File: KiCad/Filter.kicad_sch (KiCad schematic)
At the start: 25 parts, among them U5 TL074, U6 TL074

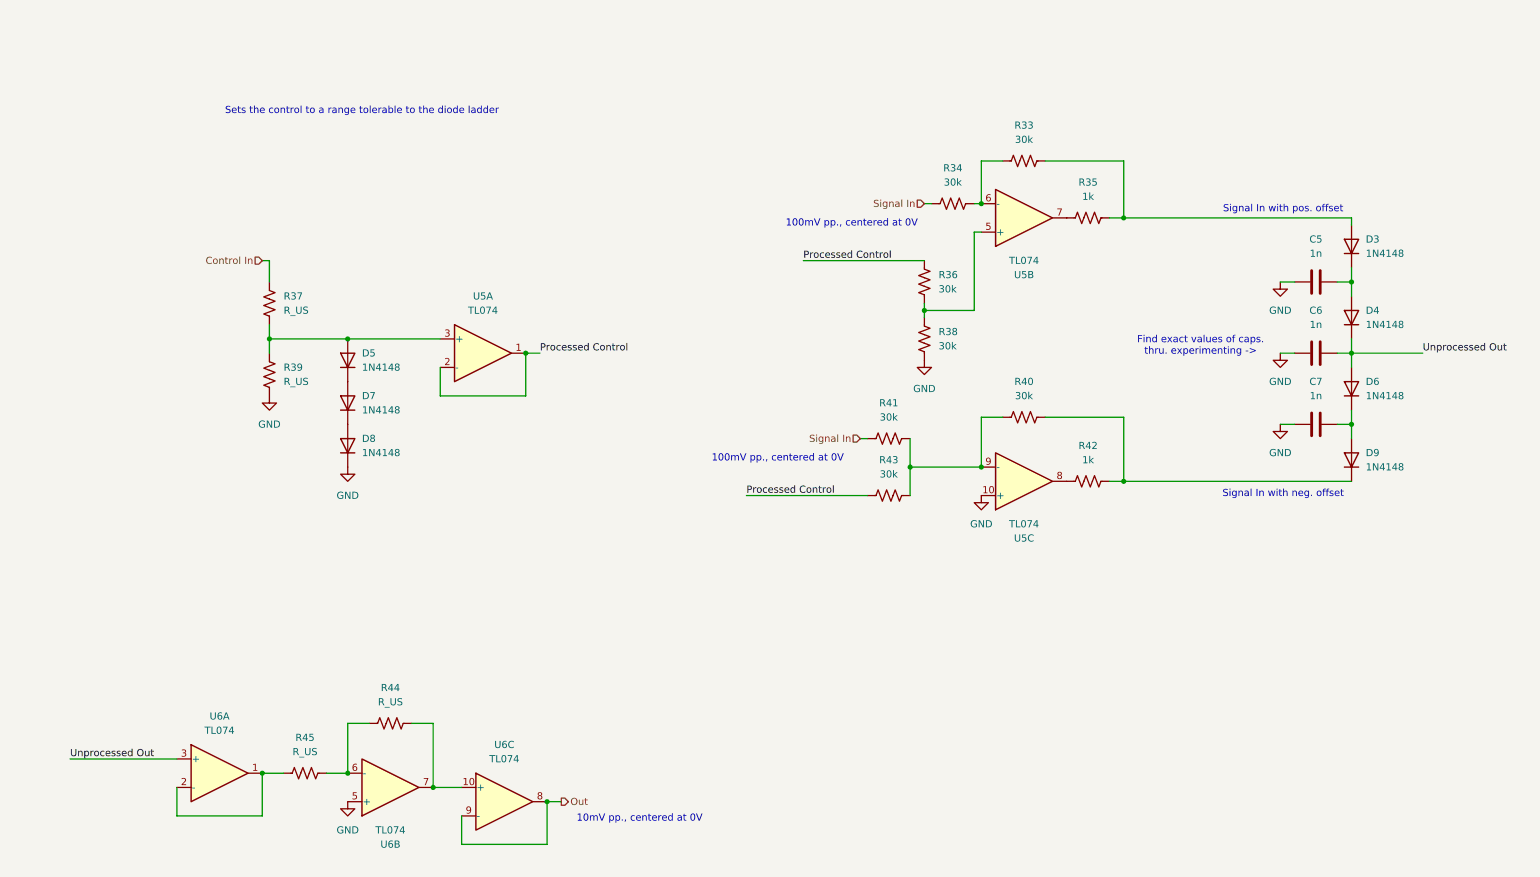
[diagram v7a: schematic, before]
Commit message: added potentiometer voltage control cct
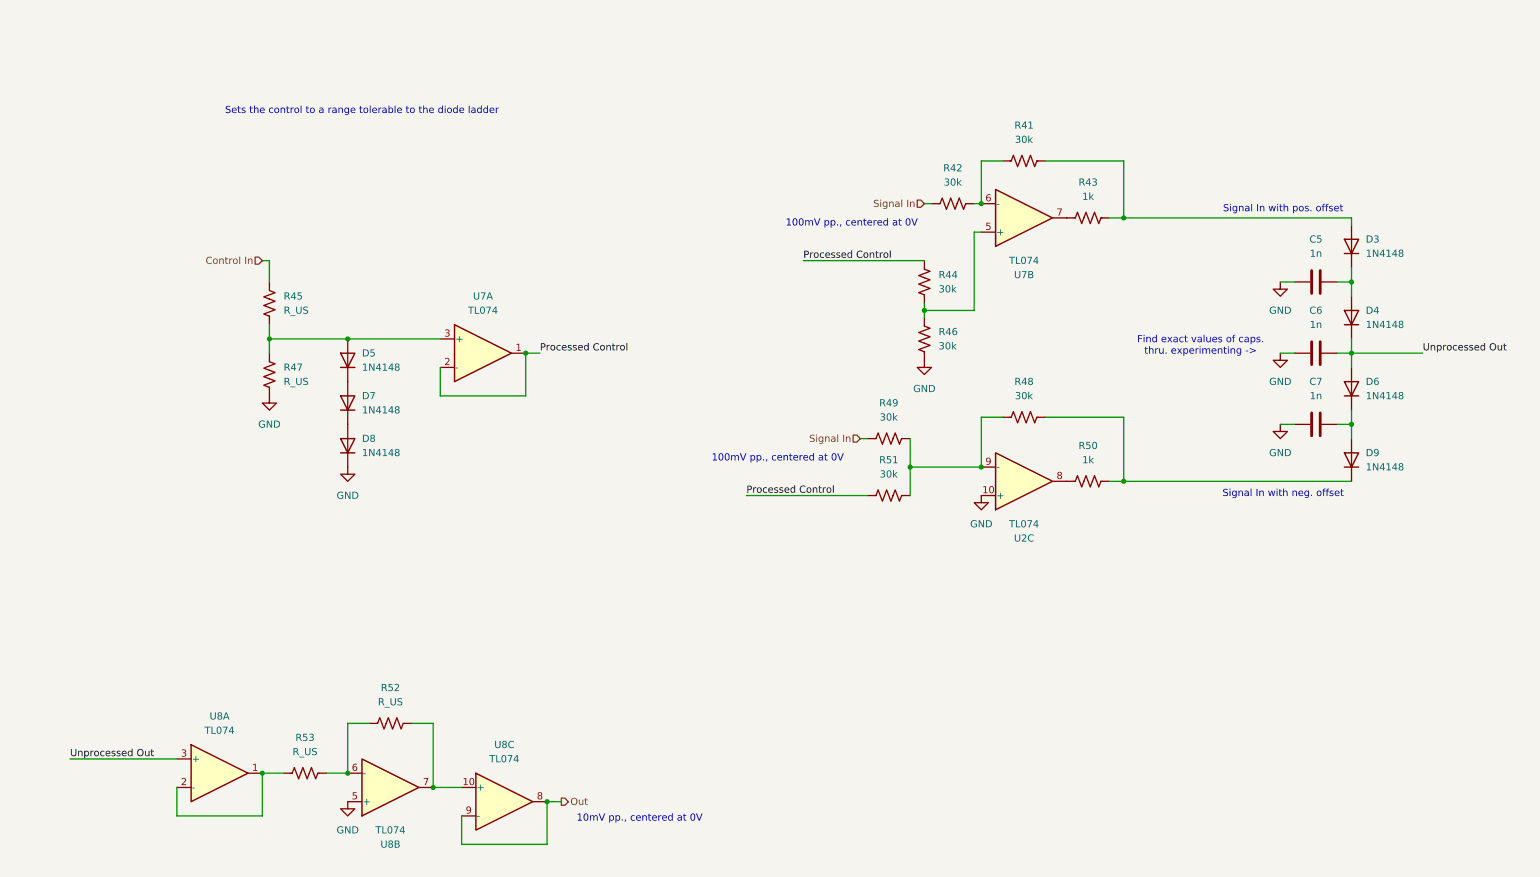
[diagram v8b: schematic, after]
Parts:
- renumbered R33 to R41, R34 to R42, R35 to R43, R36 to R44, R37 to R45, R38 to R46, R39 to R47, R40 to R48, R41 to R49, R42 to R50, R43 to R51, R44 to R52, R45 to R53, U5 to U2, U5 to U7, U6 to U8
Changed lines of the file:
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@@
 		(dnp no)
 		(fields_autoplaced yes)
-		(property "Reference" "#PWR036"
+		(property "Reference" "#PWR062"
 			(at 234.95 96.52 0)
 			(hide yes)
@@
 			(project "Electronic Trombone"
 				(path "/931827f3-33b7-460f-8885-7db258da2648/6d65ef8f-8235-46d4-95e7-69caf9b93e91"
-					(reference "#PWR036")
+					(reference "#PWR062")
 					(unit 1)
 				)
@@
 		(in_pos_files yes)
 		(dnp no)
-		(property "Reference" "U5"
+		(property "Reference" "U7"
 			(at 92.71 67.31 0)
 			(show_name no)
@@
 			(project "Electronic Trombone"
 				(path "/931827f3-33b7-460f-8885-7db258da2648/6d65ef8f-8235-46d4-95e7-69caf9b93e91"
-					(reference "U5")
+					(reference "U7")
 					(unit 1)
 				)
@@
 		(dnp no)
 		(fields_autoplaced yes)
-		(property "Reference" "R45"
+		(property "Reference" "R53"
 			(at 60.96 146.05 90)
 			(show_name no)
@@
 			(project "Electronic Trombone"
 				(path "/931827f3-33b7-460f-8885-7db258da2648/6d65ef8f-8235-46d4-95e7-69caf9b93e91"
-					(reference "R45")
+					(reference "R53")
 					(unit 1)
 				)
@@
 		(dnp no)
 		(fields_autoplaced yes)
-		(property "Reference" "R44"
+		(property "Reference" "R52"
 			(at 76.2 137.16 90)
 			(show_name no)
@@
 			(project "Electronic Trombone"
 				(path "/931827f3-33b7-460f-8885-7db258da2648/6d65ef8f-8235-46d4-95e7-69caf9b93e91"
-					(reference "R44")
+					(reference "R52")
 					(unit 1)
 				)
@@
 		(dnp no)
 		(fields_autoplaced yes)
-		(property "Reference" "#PWR034"
+		(property "Reference" "#PWR060"
 			(at 171.45 85.09 0)
 			(hide yes)
@@
 			(project "Electronic Trombone"
 				(path "/931827f3-33b7-460f-8885-7db258da2648/6d65ef8f-8235-46d4-95e7-69caf9b93e91"
-					(reference "#PWR034")
+					(reference "#PWR060")
 					(unit 1)
 				)
@@
 		(dnp no)
 		(fields_autoplaced yes)
-		(property "Reference" "R33"
+		(property "Reference" "R41"
 			(at 189.23 36.83 90)
 			(show_name no)
@@
 			(project "Electronic Trombone"
 				(path "/931827f3-33b7-460f-8885-7db258da2648/6d65ef8f-8235-46d4-95e7-69caf9b93e91"
-					(reference "R33")
+					(reference "R41")
 					(unit 1)
 				)
@@
 		(dnp no)
 		(fields_autoplaced yes)
-		(property "Reference" "#PWR032"
+		(property "Reference" "#PWR058"
 			(at 234.95 71.12 0)
 			(hide yes)
@@
 			(project "Electronic Trombone"
 				(path "/931827f3-33b7-460f-8885-7db258da2648/6d65ef8f-8235-46d4-95e7-69caf9b93e91"
-					(reference "#PWR032")
+					(reference "#PWR058")
 					(unit 1)
 				)
@@
 		(dnp no)
 		(fields_autoplaced yes)
-		(property "Reference" "R36"
+		(property "Reference" "R44"
 			(at 173.99 63.4999 0)
 			(show_name no)
@@
 			(project "Electronic Trombone"
 				(path "/931827f3-33b7-460f-8885-7db258da2648/6d65ef8f-8235-46d4-95e7-69caf9b93e91"
-					(reference "R36")
+					(reference "R44")
 					(unit 1)
 				)
@@
 		(in_pos_files yes)
 		(dnp no)
-		(property "Reference" "U6"
+		(property "Reference" "U8"
 			(at 76.2 165.1 0)
 			(show_name no)
@@
 			(project "Electronic Trombone"
 				(path "/931827f3-33b7-460f-8885-7db258da2648/6d65ef8f-8235-46d4-95e7-69caf9b93e91"
-					(reference "U6")
+					(reference "U8")
 					(unit 2)
 				)
@@
 		(dnp no)
 		(fields_autoplaced yes)
-		(property "Reference" "R37"
+		(property "Reference" "R45"
 			(at 57.15 67.3099 0)
 			(show_name no)
@@
 			(project "Electronic Trombone"
 				(path "/931827f3-33b7-460f-8885-7db258da2648/6d65ef8f-8235-46d4-95e7-69caf9b93e91"
-					(reference "R37")
+					(reference "R45")
 					(unit 1)
 				)
@@
 		(dnp no)
 		(fields_autoplaced yes)
-		(property "Reference" "R41"
+		(property "Reference" "R49"
 			(at 165.1 86.36 90)
 			(show_name no)
@@
 			(project "Electronic Trombone"
 				(path "/931827f3-33b7-460f-8885-7db258da2648/6d65ef8f-8235-46d4-95e7-69caf9b93e91"
-					(reference "R41")
+					(reference "R49")
 					(unit 1)
 				)
@@
 		(dnp no)
 		(fields_autoplaced yes)
-		(property "Reference" "#PWR037"
+		(property "Reference" "#PWR063"
 			(at 68.58 104.14 0)
 			(hide yes)
@@
 			(project "Electronic Trombone"
 				(path "/931827f3-33b7-460f-8885-7db258da2648/6d65ef8f-8235-46d4-95e7-69caf9b93e91"
-					(reference "#PWR037")
+					(reference "#PWR063")
 					(unit 1)
 				)
@@
 		(dnp no)
 		(fields_autoplaced yes)
-		(property "Reference" "R42"
+		(property "Reference" "R50"
 			(at 200.66 93.98 90)
 			(show_name no)
@@
 			(project "Electronic Trombone"
 				(path "/931827f3-33b7-460f-8885-7db258da2648/6d65ef8f-8235-46d4-95e7-69caf9b93e91"
-					(reference "R42")
+					(reference "R50")
 					(unit 1)
 				)
@@
 		(in_pos_files yes)
 		(dnp no)
-		(property "Reference" "U6"
+		(property "Reference" "U8"
 			(at 45.72 142.24 0)
 			(show_name no)
@@
 			(project "Electronic Trombone"
 				(path "/931827f3-33b7-460f-8885-7db258da2648/6d65ef8f-8235-46d4-95e7-69caf9b93e91"
-					(reference "U6")
+					(reference "U8")
 					(unit 1)
 				)
@@
 		(in_pos_files yes)
 		(dnp no)
-		(property "Reference" "U5"
+		(property "Reference" "U2"
 			(at 189.23 110.49 0)
 			(show_name no)
@@
 			(project "Electronic Trombone"
 				(path "/931827f3-33b7-460f-8885-7db258da2648/6d65ef8f-8235-46d4-95e7-69caf9b93e91"
-					(reference "U5")
+					(reference "U2")
 					(unit 3)
 				)
@@
 		(dnp no)
 		(fields_autoplaced yes)
-		(property "Reference" "#PWR038"
+		(property "Reference" "#PWR064"
 			(at 181.61 109.22 0)
 			(hide yes)
@@
 			(project "Electronic Trombone"
 				(path "/931827f3-33b7-460f-8885-7db258da2648/6d65ef8f-8235-46d4-95e7-69caf9b93e91"
-					(reference "#PWR038")
+					(reference "#PWR064")
 					(unit 1)
 				)
@@
 		(in_pos_files yes)
 		(dnp no)
-		(property "Reference" "U6"
+		(property "Reference" "U8"
 			(at 96.52 147.32 0)
 			(show_name no)
@@
 			(project "Electronic Trombone"
 				(path "/931827f3-33b7-460f-8885-7db258da2648/6d65ef8f-8235-46d4-95e7-69caf9b93e91"
-					(reference "U6")
+					(reference "U8")
 					(unit 3)
 				)
@@
 		(dnp no)
 		(fields_autoplaced yes)
-		(property "Reference" "#PWR035"
+		(property "Reference" "#PWR061"
 			(at 54.61 91.44 0)
 			(hide yes)
@@
 			(project "Electronic Trombone"
 				(path "/931827f3-33b7-460f-8885-7db258da2648/6d65ef8f-8235-46d4-95e7-69caf9b93e91"
-					(reference "#PWR035")
+					(reference "#PWR061")
 					(unit 1)
 				)
@@
 		(dnp no)
 		(fields_autoplaced yes)
-		(property "Reference" "R40"
+		(property "Reference" "R48"
 			(at 189.23 82.55 90)
 			(show_name no)
@@
 			(project "Electronic Trombone"
 				(path "/931827f3-33b7-460f-8885-7db258da2648/6d65ef8f-8235-46d4-95e7-69caf9b93e91"
-					(reference "R40")
+					(reference "R48")
 					(unit 1)
 				)
@@
 		(in_pos_files yes)
 		(dnp no)
-		(property "Reference" "U5"
+		(property "Reference" "U7"
 			(at 189.23 63.5 0)
 			(show_name no)
@@
 			(project "Electronic Trombone"
 				(path "/931827f3-33b7-460f-8885-7db258da2648/6d65ef8f-8235-46d4-95e7-69caf9b93e91"
-					(reference "U5")
+					(reference "U7")
 					(unit 2)
 				)
@@
 		(dnp no)
 		(fields_autoplaced yes)
-		(property "Reference" "#PWR033"
+		(property "Reference" "#PWR059"
 			(at 234.95 83.82 0)
 			(hide yes)
@@
 			(project "Electronic Trombone"
 				(path "/931827f3-33b7-460f-8885-7db258da2648/6d65ef8f-8235-46d4-95e7-69caf9b93e91"
-					(reference "#PWR033")
+					(reference "#PWR059")
 					(unit 1)
 				)
@@
 		(dnp no)
 		(fields_autoplaced yes)
-		(property "Reference" "#PWR039"
+		(property "Reference" "#PWR065"
 			(at 68.58 163.83 0)
 			(hide yes)
@@
 			(project "Electronic Trombone"
 				(path "/931827f3-33b7-460f-8885-7db258da2648/6d65ef8f-8235-46d4-95e7-69caf9b93e91"
-					(reference "#PWR039")
+					(reference "#PWR065")
 					(unit 1)
 				)
@@
 		(dnp no)
 		(fields_autoplaced yes)
-		(property "Reference" "R39"
+		(property "Reference" "R47"
 			(at 57.15 80.0099 0)
 			(show_name no)
@@
 			(project "Electronic Trombone"
 				(path "/931827f3-33b7-460f-8885-7db258da2648/6d65ef8f-8235-46d4-95e7-69caf9b93e91"
-					(reference "R39")
+					(reference "R47")
 					(unit 1)
 				)
@@
 		(dnp no)
 		(fields_autoplaced yes)
-		(property "Reference" "R43"
+		(property "Reference" "R51"
 			(at 165.1 96.52 90)
 			(show_name no)
@@
 			(project "Electronic Trombone"
 				(path "/931827f3-33b7-460f-8885-7db258da2648/6d65ef8f-8235-46d4-95e7-69caf9b93e91"
-					(reference "R43")
+					(reference "R51")
 					(unit 1)
 				)
@@
 		(dnp no)
 		(fields_autoplaced yes)
-		(property "Reference" "R38"
+		(property "Reference" "R46"
 			(at 173.99 73.6599 0)
 			(show_name no)
@@
 			(project "Electronic Trombone"
 				(path "/931827f3-33b7-460f-8885-7db258da2648/6d65ef8f-8235-46d4-95e7-69caf9b93e91"
-					(reference "R38")
+					(reference "R46")
 					(unit 1)
 				)
@@
 		(dnp no)
 		(fields_autoplaced yes)
-		(property "Reference" "R34"
+		(property "Reference" "R42"
 			(at 176.53 44.45 90)
 			(show_name no)
@@
 			(project "Electronic Trombone"
 				(path "/931827f3-33b7-460f-8885-7db258da2648/6d65ef8f-8235-46d4-95e7-69caf9b93e91"
-					(reference "R34")
+					(reference "R42")
 					(unit 1)
 				)
@@
 		(dnp no)
 		(fields_autoplaced yes)
-		(property "Reference" "R35"
+		(property "Reference" "R43"
 			(at 200.66 46.99 90)
 			(show_name no)
@@
 			(project "Electronic Trombone"
 				(path "/931827f3-33b7-460f-8885-7db258da2648/6d65ef8f-8235-46d4-95e7-69caf9b93e91"
-					(reference "R35")
-					(unit 1)
-				)
+					(reference "R43")
+					(unit 1)
+				)
